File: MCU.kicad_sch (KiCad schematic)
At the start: 26 parts, among them J3 ST_LINK, SW1 Reset, U1 STM32G070CBT6, U5 LM4040DBZ-3, Y1 FC-135R_32.7680KA-AG0

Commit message: KiCad 0.2v
Schematics done.
Have to assign footprints to corresponding components.
Completely rework PCB.
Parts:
- removed C12, C14: 12.5pF, Capacitor_SMD:C_0603_1608Metric, symbol Device:C_Small
- removed C13: 220nF, Capacitor_SMD:C_0603_1608Metric, symbol Device:C_Small
- removed C4, C5, C6: 0.1uF, Capacitor_SMD:C_0603_1608Metric, symbol Device:C_Small
- removed D2: LED, symbol Device:LED
- removed D6: ASMT-YTD7-0AA02, LED_ASMT-YTD7-0AA02, symbol test:ASMT-YTD7-0AA02
- removed J3: ST_LINK, Connector_PinSocket_2.54mm:PinSocket_1x04_P2.54mm_Vertical, symbol Connector_Generic:Conn_01x04
- removed R2: 12k, Resistor_SMD:R_0603_1608Metric, symbol Device:R_Small
- removed U1: STM32G070CBT6, LQFP-48, symbol test:STM32G070CBT6
- added C24, C25, C26: 0.1uF, Capacitor_SMD:C_0603_1608Metric, symbol Device:C_Small
- added C27, C29: 12.5pF, Capacitor_SMD:C_0603_1608Metric, symbol Device:C_Small
- added C28: 220nF, Capacitor_SMD:C_0603_1608Metric, symbol Device:C_Small
- added D2: RGB, footprints:LED_ASMT-YTD7-0AA02, symbol test:ASMT-YTD7-0AA02
- added D6: LED, symbol Device:LED
- added J8: ST_LINK, Connector_PinSocket_2.54mm:PinSocket_1x04_P2.54mm_Vertical, symbol Connector_Generic:Conn_01x04
- added R5: 12k, Resistor_SMD:R_0603_1608Metric, symbol Device:R_Small
- added U4: STM32G070CBT6, LQFP-48, symbol test:STM32G070CBT6
- R10: value R_Small -> 20
- R11, R12, R13, R14: value R_Small -> 120
- R8: value R_Small -> 150
- R9: value R_Small -> 50
- Y1: footprint XTAL_FC-135R_32.7680KA-AG0 -> footprints:XTAL_FC-135R_32.7680KA-AG0
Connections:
- net GND: now also C24.2, C25.2, C26.2, C27.1, C28.2, C29.2, J8.1 (Pin_1), R5.2, U4.7 (VSS)
- net GPS_RX: now also U4.12 (PA1)
- net GPS_TX: now also U4.11 (PA0)
- net GSM_CTS: now also U4.46 (PB7)
- net GSM_GPIO1_INT: now also U4.43 (PB4)
- net GSM_PWR: now also U4.42 (PB3)
- net GSM_RST: now also U4.44 (PB5)
- net GSM_RTS: now also U4.45 (PB6)
- net GSM_RX: now also U4.48 (PB9)
- net GSM_TX: now also U4.47 (PB8)
- net LED0: now also D6.2 (A), U4.38 (PD0); no longer D5.2 (A)
- net LED1: now also D5.2 (A), U4.39 (PD1); no longer D4.2 (A)
- net LED2: now also D4.2 (A), U4.40 (PD2); no longer D3.2 (A)
- net LED3: now also D3.2 (A), U4.41 (PD3)
- net MB_RX: now also U4.14 (PA3)
- net MB_TX: now also U4.13 (PA2)
- net OSC32_IN: now also C27.2, U4.2 (PC14-OSC32_IN)
- net OSC32_OUT: now also C29.1, U4.3 (PC15-OSC32_OUT)
- net RF_DIO0: now also U4.20 (PB1)
- net RF_DIO1: now also U4.21 (PB2)
- net RF_IRQ: now also U4.22 (PB10)
- net RF_MISO: now also U4.17 (PA6)
- net RF_MOSI: now also U4.18 (PA7)
- net RF_NSS: now also U4.15 (PA4)
- net RF_RST: now also U4.19 (PB0)
- net RF_SCK: now also U4.16 (PA5)
- net RGB_BLUE: now also D2.6, U4.27 (PB15)
- net RGB_GREEN: now also D2.5, U4.26 (PB14)
- net RGB_RED: now also D2.4, U4.25 (PB13)
- net RX: now also U4.29 (PA9)
- net SW_CLK: now also J8.2 (Pin_2), R5.1, U4.35 (PA13)
- net SW_IO: now also J8.3 (Pin_3), U4.36 (PA14-BOOT0)
- net TX: now also U4.32 (PA10)
- net VREF+: now also C26.1, U4.5 (VREF+)
- net ~{RST}: now also C28.1, J8.4 (Pin_4), U4.10 (PF2-NRST)
- net at R13.1: now also D5.1 (K)
- net at R11.1: now also D3.1 (K); no longer D5.1 (K)
- net at R14.1: now also D6.1 (K)
- net at R9.1: now also D2.2; no longer D3.1 (K)
- net at R8.1: now also D2.3
- net at D4.1 (K): now also R12.1; no longer R10.1
- net 3.3V renamed +3V3
- net +3V3: now also C24.1, C25.1, U4.4 (VBAT), U4.6 (VDD)
- new net: D2.1, R10.1

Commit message: KiCad 0.3v
Improved aesthetics.
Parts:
- removed D2: RGB, footprints:LED_ASMT-YTD7-0AA02, symbol test:ASMT-YTD7-0AA02
- removed Y1: FC-135R_32.7680KA-AG0, footprints:XTAL_FC-135R_32.7680KA-AG0, symbol test:FC-135R_32.7680KA-AG0
- added D2: ASMT-YTD7-0AA02, LED_ASMT-YTD7-0AA02, symbol schematics:ASMT-YTD7-0AA02
- added Y1: FC-135R_32.7680KA-AG0, XTAL_FC-135R_32.7680KA-AG0, symbol schematics:FC-135R_32.7680KA-AG0
- C28: value 220nF -> 0.1uF
- D3, D4, D5, D6: footprint (none) -> LED_SMD:LED_0603_1608Metric
- R10: value 20 -> 120; footprint (none) -> Resistor_SMD:R_0603_1608Metric
- R11, R12, R13, R14: footprint (none) -> Resistor_SMD:R_0603_1608Metric
- R6: value R_Small -> 12k; footprint (none) -> Resistor_SMD:R_0603_1608Metric
- R8: value 150 -> 120; footprint (none) -> Resistor_SMD:R_0603_1608Metric
- R9: value 50 -> 120; footprint (none) -> Resistor_SMD:R_0603_1608Metric
- U4: symbol test:STM32G070CBT6 -> schematics:STM32G070CBT6
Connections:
- net OSC32_IN: now also Y1.1
- net OSC32_OUT: now also Y1.2
- net RGB_BLUE: now also D2.6
- net RGB_GREEN: now also D2.5
- net RGB_RED: now also D2.4
- net at R9.1: now also D2.2
- net at R8.1: now also D2.3
- net at R10.1: now also D2.1
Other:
- note added: "Decoupling cap and refrence voltage"
- note added: "LED array"
- note added: "MCU"
- note added: "Programmer connector"
- note added: "RGB"
- note added: "RTC oscillator"
- note added: "Reset"
- moved on the sheet: C24, C25, C26, C27, C28, C29, D3, D4, D5, D6, J8, R10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

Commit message: 0.1v COM_PCB KiCad
First iteration of COM PCB.
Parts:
- removed C25, C26, C28: 0.1uF, Capacitor_SMD:C_0603_1608Metric, symbol Device:C_Small
- removed D2: ASMT-YTD7-0AA02, LED_ASMT-YTD7-0AA02, symbol schematics:ASMT-YTD7-0AA02
- removed J8: ST_LINK, Connector_PinSocket_2.54mm:PinSocket_1x04_P2.54mm_Vertical, symbol Connector_Generic:Conn_01x04
- removed R10, R8, R9: 120, Resistor_SMD:R_0603_1608Metric, symbol Device:R_Small
- removed R6: 12k, Resistor_SMD:R_0603_1608Metric, symbol Device:R_Small
- removed SW1: Reset, button:little_button, symbol Switch:SW_Push
- removed U4: STM32G070CBT6, LQFP-48, symbol schematics:STM32G070CBT6
- removed U5: LM4040DBZ-3, Package_TO_SOT_SMD:SOT-23, symbol Reference_Voltage:LM4040DBZ-3
- added U4: STM32G071GBU, Package_DFN_QFN:QFN-28_4x4mm_P0.5mm, symbol schematics:STM32G071GBU
- Y1: footprint XTAL_FC-135R_32.7680KA-AG0 -> footprints:XTAL_FC-135R_32.7680KA-AG0
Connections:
- net +3V3: now also U4.3 (VDD)
- net GND: now also D3.1 (K), D4.1 (K), D5.1 (K), D6.1 (K), U4.4 (VSS); no longer R11.2, R12.2, R13.2, R14.2
- net GPS_RX: now also U4.9 (PA3)
- net GPS_TX: now also U4.8 (PA2)
- net GSM_GPIO1_INT: now also U4.23 (PB3)
- net GSM_PWR: now also U4.24 (PB4)
- net GSM_RST: now also U4.22 (PA15)
- net GSM_RX: now also U4.27 (PB7)
- net GSM_TX: now also U4.26 (PB6)
- net LED0: now also R14.1, U4.19 (PA12[10]); no longer D6.2 (A)
- net LED1: now also R13.1, U4.18 (PA11[9]); no longer D5.2 (A)
- net LED2: now also R12.1, U4.25 (PB5); no longer D4.2 (A)
- net LED3: now also R11.1, U4.10 (PA4); no longer D3.2 (A)
- net MB_RX: now also U4.7 (PA1)
- net MB_TX: now also U4.6 (PA0)
- net OSC32_IN: now also U4.2 (PC15)
- net OSC32_OUT: now also U4.1 (PC14)
- net RF_DIO0: now also U4.16 (PA8)
- net RF_IRQ: now also U4.15 (PB1)
- net RF_MISO: now also U4.12 (PA6)
- net RF_MOSI: now also U4.13 (PA7)
- net RF_NSS: now also U4.14 (PB0)
- net RF_RST: now also U4.17 (PC6)
- net RF_SCK: now also U4.11 (PA5)
- net SW_CLK: now also U4.21 (PA14-BOOT)
- net SW_IO: now also U4.20 (PA13)
- net ~{RST}: now also U4.5 (PF2-NRST)
- new net: D4.2 (A), R12.2
- new net: D5.2 (A), R13.2
- new net: D6.2 (A), R14.2
- new net: D3.2 (A), R11.2
- new net DEBUG_TX: U4.28 (PB8)
- no-connect marks 11 -> 0
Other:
- note added: "Decoupling cap"
- note removed: "Decoupling cap and refrence voltage"
- note removed: "Programmer connector"
- note removed: "RGB"
- moved on the sheet: C24, C27, C29, D3, D4, D5, D6, R11, R12, R13, R14, R7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

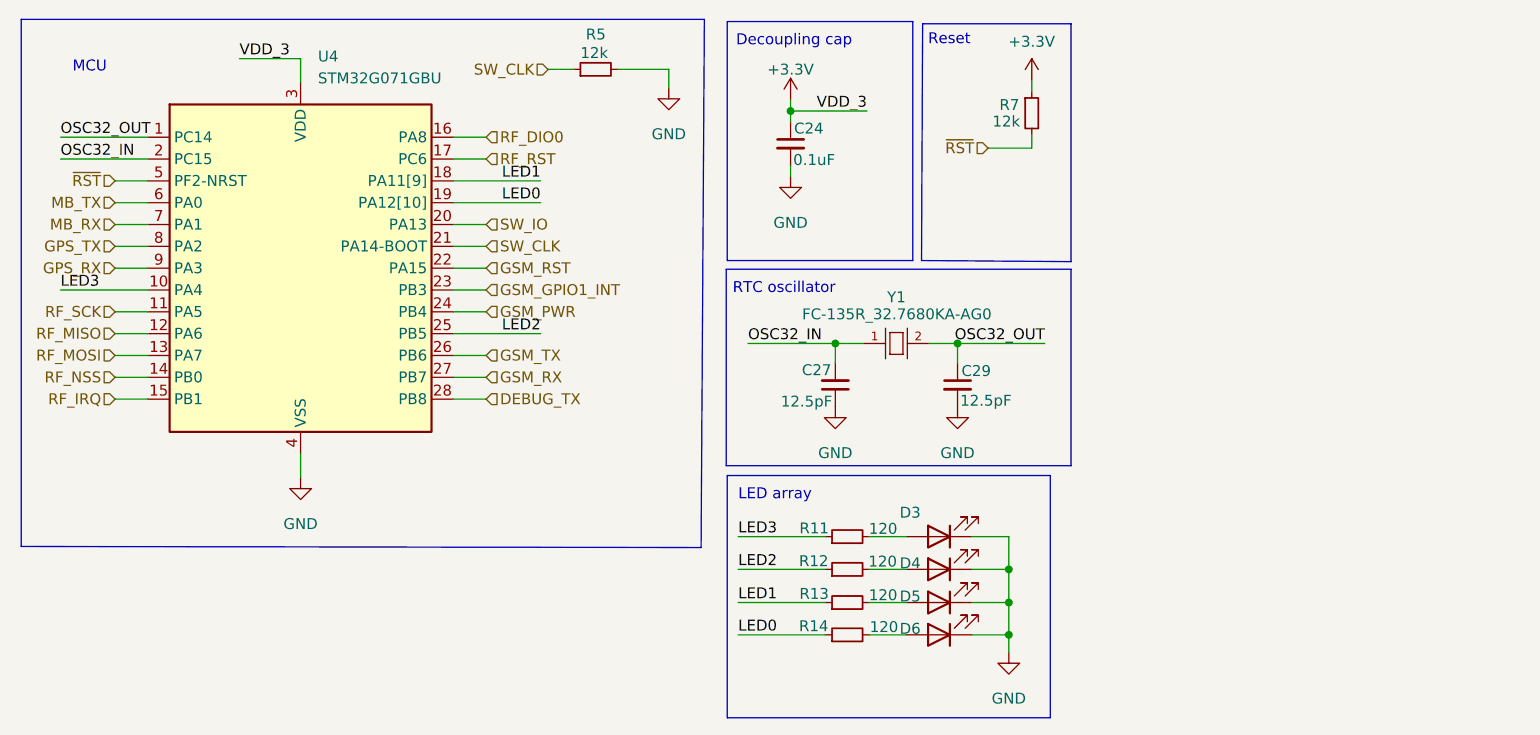
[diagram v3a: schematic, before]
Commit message: solved issues
Crystal changes and some routing.
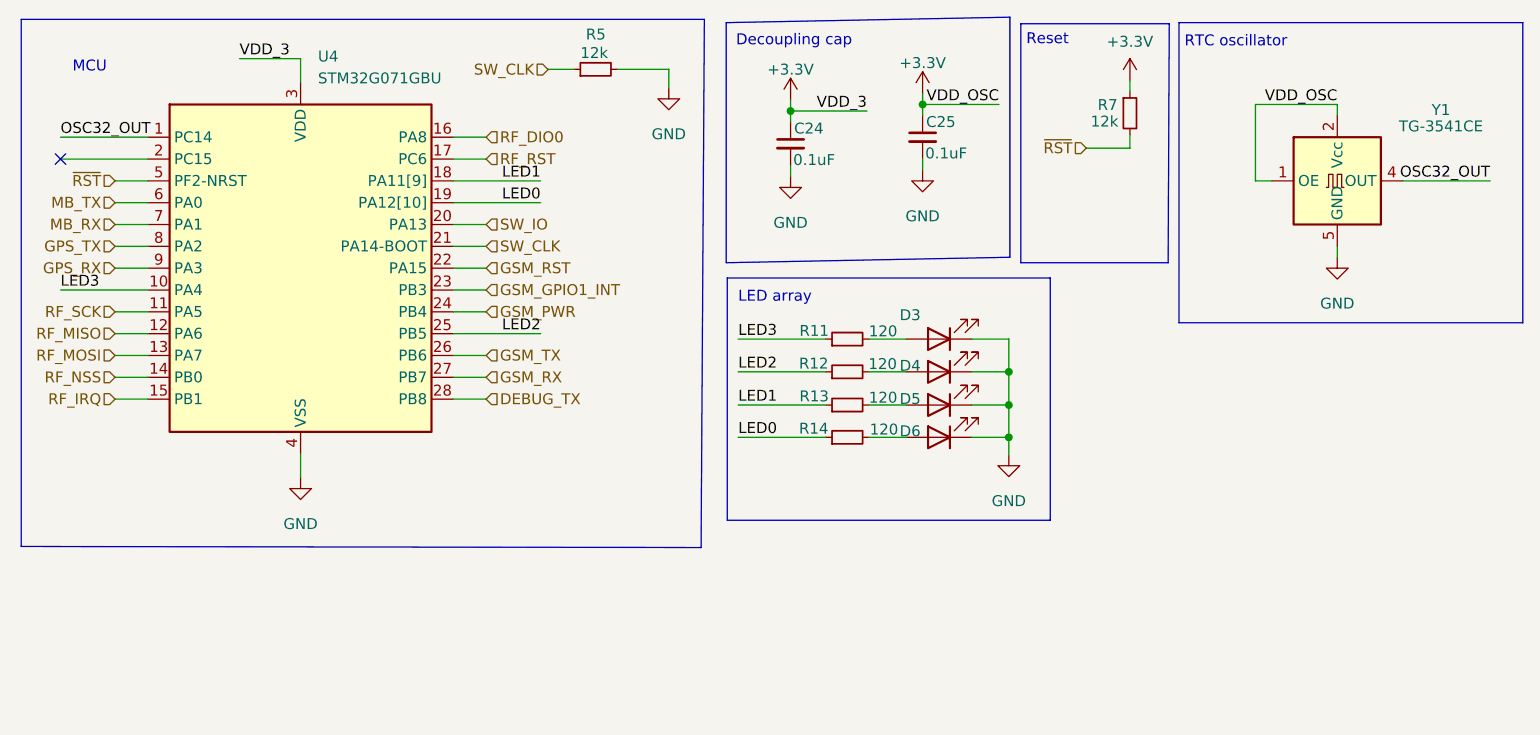
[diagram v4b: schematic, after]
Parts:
- removed C27, C29: 12.5pF, Capacitor_SMD:C_0603_1608Metric, symbol Device:C_Small
- removed Y1: FC-135R_32.7680KA-AG0, footprints:XTAL_FC-135R_32.7680KA-AG0, symbol schematics:FC-135R_32.7680KA-AG0
- added C25: 0.1uF, Capacitor_SMD:C_0603_1608Metric, symbol Device:C_Small
- added Y1: TG-3541CE, footprints:Oscillator_SMD_SeikoEpson_TG-3541CE_3.2x2.5mm, symbol schematics:TG-3541CE
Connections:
- net +3V3: now also C25.1, Y1.1 (OE), Y1.2 (Vcc), Y1.3 (Vcc)
- net GND: now also C25.2, Y1.5 (GND), Y1.7 (GND), Y1.8 (GND), Y1.9 (GND)
- net OSC32_OUT: now also Y1.4 (OUT)
- net OSC32_IN: no longer names the net of U4.2 (PC15)
- no-connect marks 0 -> 1
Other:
- moved on the sheet: D3, D4, D5, D6, R11, R12, R13, R14, R7

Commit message: V1
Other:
- company: (none) -> BASEMENT
- title: (none) -> STM32 MCU
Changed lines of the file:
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@@
 (kicad_sch (version 20211123) (generator eeschema)
   (paper "A4")
+  (title_block
+    (title "STM32 MCU")
+    (date "%%date%%")
+    (rev "%%version%%")
+    (company "BASEMENT")
+  )
   (junction (at 120.65 25.4) (diameter 0) (color 0 0 0 0)
   )
